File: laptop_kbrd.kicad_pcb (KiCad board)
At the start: 2 copper layers, 111.5 x 18 mm, 62 parts, among them CON1 AVR-ISP-6-DR, K1 CASE_OPEN, Q1 MOSFET_N, Q2 MOSFET_N, Q3 MOSFET_N, Q4 MOSFET_N, Q5 MOSFET_N, Q6 MOSFET_N, Q7 MOSFET_N, Q8 ALS_PT19, SW1 MCU_RST, SW2 BT_ASSCN, SW3 POWER, U1 ATMEGA32U4-AU, U2 RT9706, U3 RCLAMP0502B, U4 0WX4JF, U5 XF2M-3015-1A, X1 XTAL 16MHz

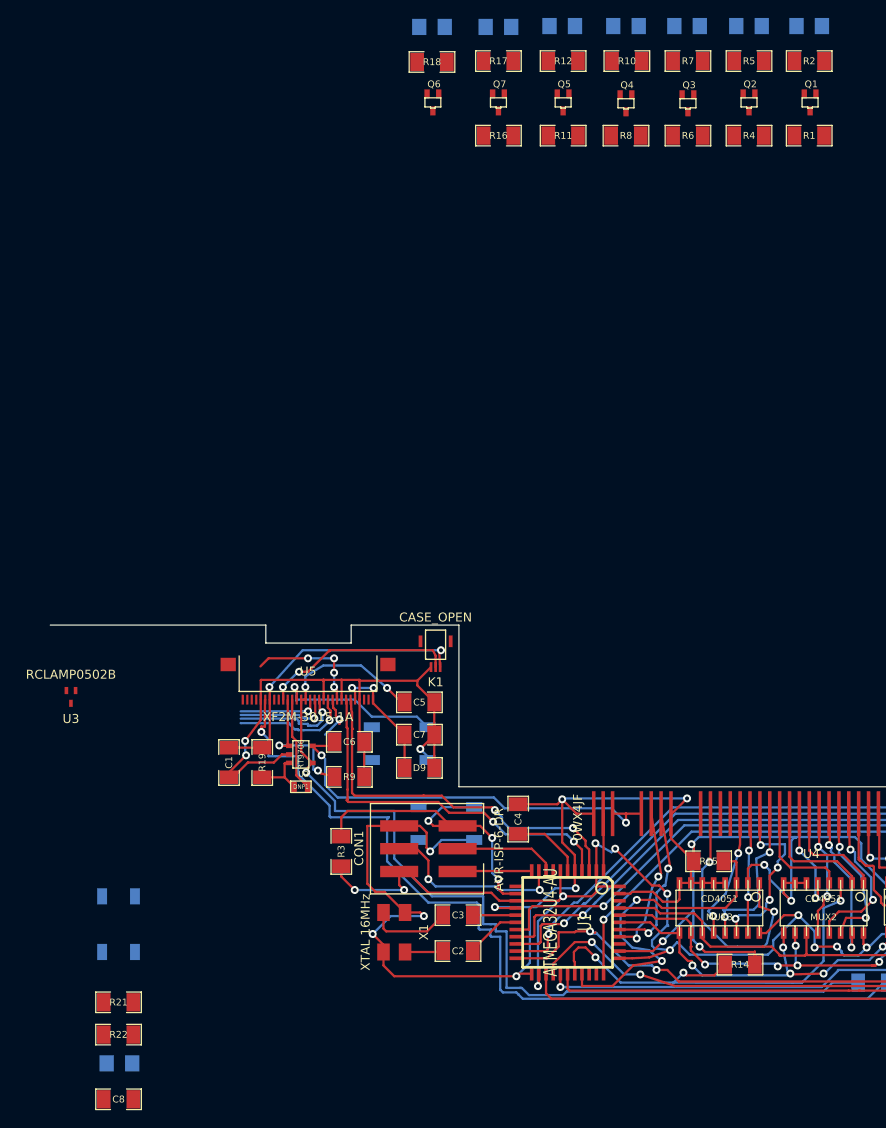
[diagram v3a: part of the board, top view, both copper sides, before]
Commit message: Removed RCLAMP
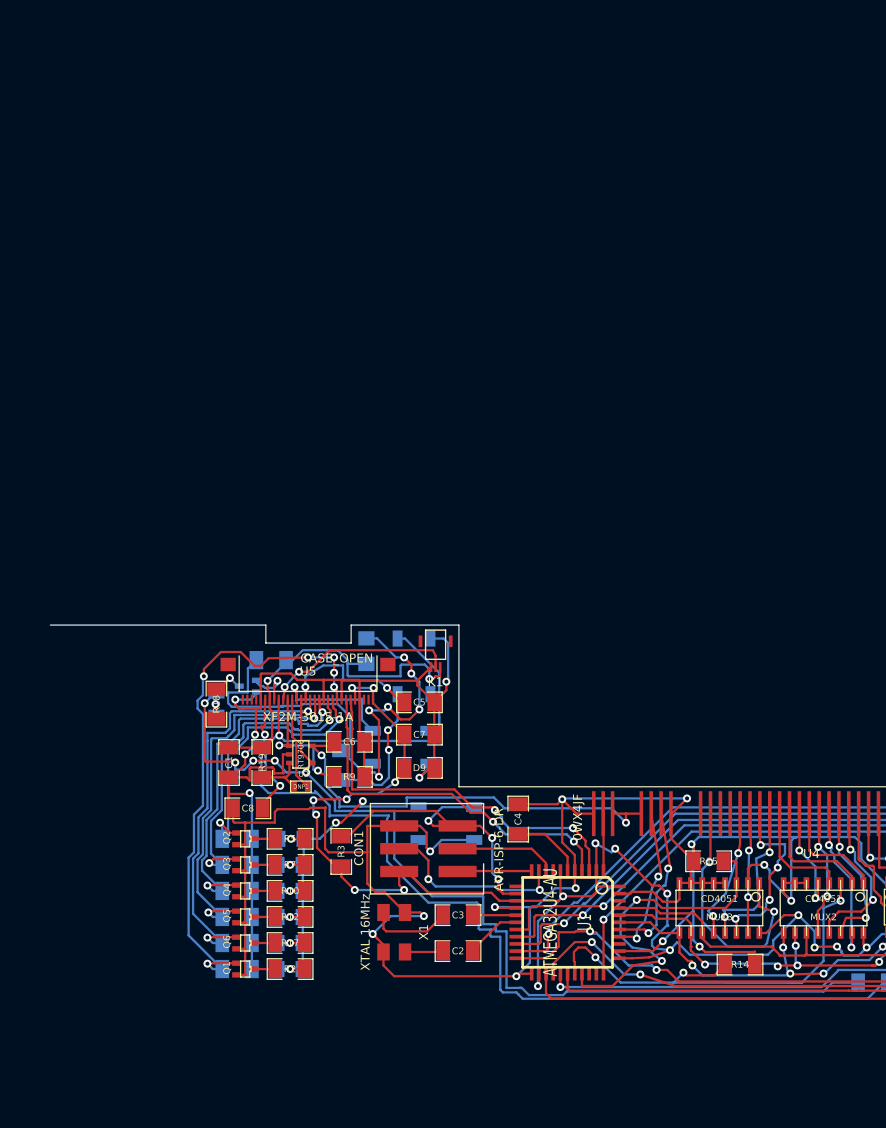
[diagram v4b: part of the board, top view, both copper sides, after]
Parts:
- removed U3: RCLAMP0502B, SOT523
- Q7, R1, R11, R16, R21, R22, R4, R6, R8: moved to B.Cu
- moved D1 119.9 mm to (91.2, 136.3), turned to 180 degrees
- moved R2 116.5 mm to (91.2, 136.3), turned to 180 degrees
- moved Q1 115.2 mm to (86.2, 136.3), turned to 90 degrees
- moved R1 112.6 mm to (85.3, 136.3)
- moved D6 104.6 mm to (91.2, 133.4), turned to 180 degrees
- moved D2 103.9 mm to (91.3, 121.8), turned to 180 degrees
- moved D5 103.7 mm to (91.2, 130.5), turned to 180 degrees
- moved D3 103.3 mm to (91.2, 124.7), turned to 180 degrees
- moved D4 103.3 mm to (91.2, 127.6), turned to 180 degrees
- moved R17 100.9 mm to (91.2, 133.4), turned to 180 degrees
- moved R5 100.6 mm to (91.2, 121.8), turned to 180 degrees
- moved R12 100.0 mm to (91.2, 130.5), turned to 180 degrees
- moved R7 99.9 mm to (91.2, 124.7), turned to 180 degrees
- moved R10 99.7 mm to (91.2, 127.6), turned to 180 degrees
- moved Q2 99.4 mm to (86.2, 121.8), turned to 90 degrees
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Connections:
- SW3 pad 3: (no net) -> /CHG_PWRSWITCH
- SW3 pad 4: /CHG_PWRSWITCH -> (no net)
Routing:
- net GND: track 320.2 -> 415.5 mm, vias 21 -> 24
- net /KEY_ROW1: track 0.00 -> 72.1 mm, vias 0 -> 2
- net /FPGA CLK: track 13.3 -> 62.5 mm, vias 4 -> 6
- net /FPGA CS: track 8.90 -> 45.2 mm, vias 1 -> 2
- net /FPGA HOLD: track 10.6 -> 42.5 mm, vias 1 -> 2
- net N-0000064: track 0.00 -> 31.7 mm, vias 0 -> 6
- net /FPGA MOSI: track 12.4 -> 40.3 mm, vias 1 -> 2
- net /FPGA WP: track 5.94 -> 32.3 mm, vias 1 -> 2
- net VDD: track 47.1 -> 72.9 mm, vias 2 -> 4
- net /FPGA MISO: track 13.3 -> 36.1 mm, vias 1 -> 2
- net /5V_DELAYED: track 107.2 -> 129.9 mm, vias 3 -> 7
- net VCC: track 148.2 -> 169.0 mm, vias 15 -> 19
- net N-0000065: track 0.00 -> 15.6 mm, vias 0 -> 2
- net /3.3V_DELAYED: track 33.7 -> 40.6 mm
- net /EPIT1_EPIT0: track 0.00 -> 5.64 mm, vias 0 -> 1
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
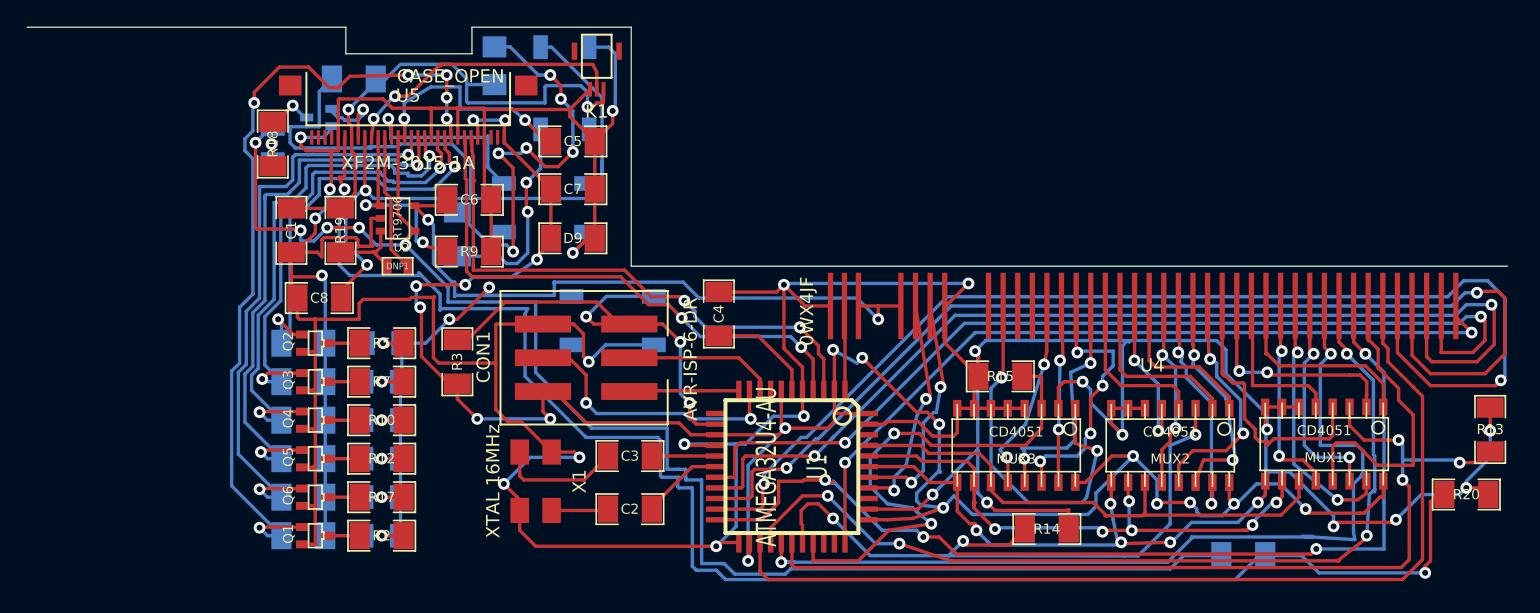
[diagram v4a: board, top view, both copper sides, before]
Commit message: Added lidsense. Mounting holes.
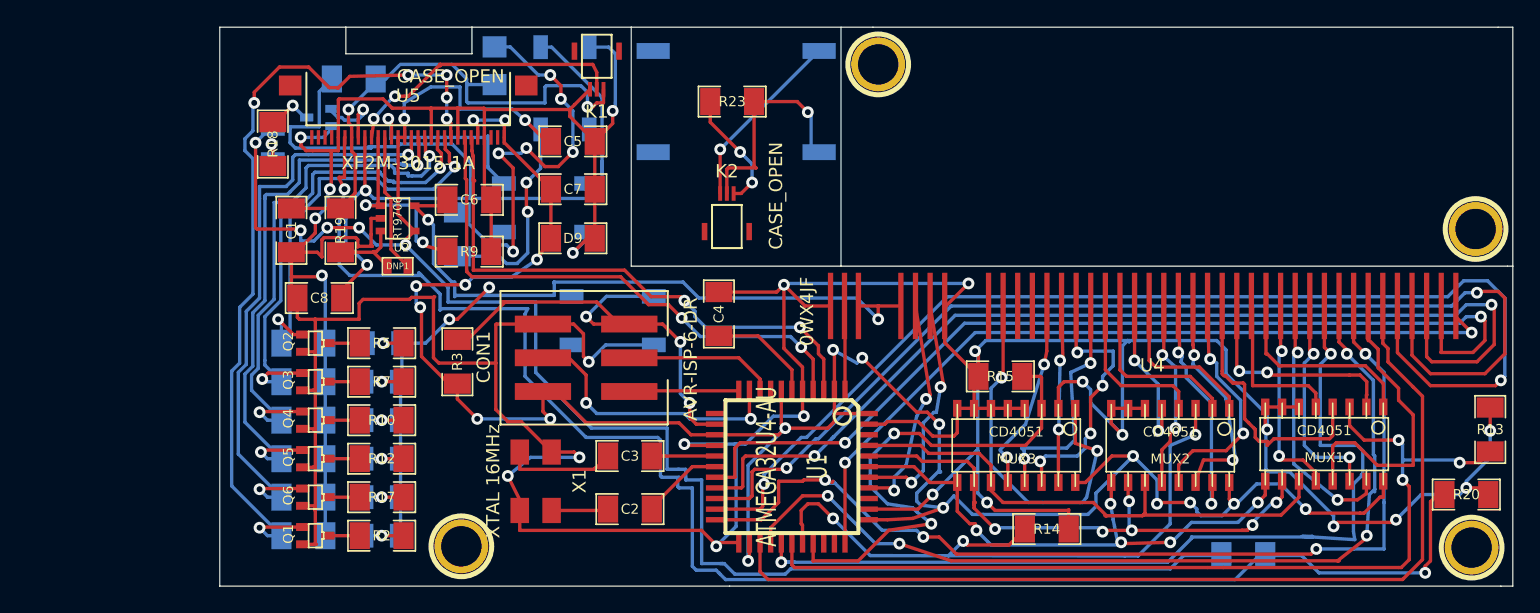
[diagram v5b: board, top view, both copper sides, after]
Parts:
- added ?: P***, 1pin, F.Cu at (173.3, 137.2)
- added ?: P***, 1pin, F.Cu at (97.2, 137.1)
- added ?: P***, 1pin, F.Cu at (128.6, 100.8)
- added ?: P***, 1pin, F.Cu at (173.6, 113.2)
- added K2: CASE_OPEN, 3pin_FPC, F.Cu at (117.2, 112.2)
- added R23: 47K, SM1206, F.Cu at (117.6, 103.6)
- added SW4: CASE_PUSH, PUSH_BT, B.Cu at (117.9, 103.6)
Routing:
- net N-0000060: track 0.00 -> 16.6 mm, vias 0 -> 1
- net N-0000059: track 0.00 -> 13.6 mm, vias 0 -> 1
- net N-0000057: track 0.00 -> 9.14 mm, vias 0 -> 2
- net N-0000010: track 9.32 -> 8.43 mm
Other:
- board size 111.5 x 18 mm -> 97.4 x 42.1 mm

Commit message: New components for the LCD controller.
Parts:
- added C10: 22pF, SM1206, F.Cu at (232.1, 176.1)
- added C11: 22pF, SM1206, F.Cu at (345.6, 72.3)
- added C12: 22pF, SM1206, F.Cu at (354.9, 72.8)
- added C13: 1uF, SM1206, F.Cu at (238.3, 165.2)
- added C14: 1uF, SM1206, F.Cu at (345.6, 69.7)
- added C15: 0.1uF, SM1206, F.Cu at (303.3, 217.6)
- added C16: 2.2nF, SM1206, F.Cu at (305.4, 213.0)
- added C17: 0.1uF, SM1206, F.Cu at (309.1, 197.9)
- added C18: 2.2nF, SM1206, F.Cu at (306.2, 223.1)
- added C19: 100pF, SM1206, F.Cu at (325.4, 222.6)
- added C20: 22pF, SM1206, F.Cu at (263.9, 171.2)
- added C21: 2.2nF, SM1206, F.Cu at (315.8, 228.8)
- added C22: 22pF, SM1206, F.Cu at (263.9, 168.5)
- added C23: 0.1uF, SM1206, F.Cu at (331.9, 217.0)
- added C24: 0.1uF, SM1206, F.Cu at (210.6, 176.4)
- added C9: 22pF, SM1206, F.Cu at (225.3, 176.1)
- added CON2: AVR-ISP-6-DR, AVR_6_SMD, B.Cu at (245.6, 165.2)
- added CON3: AVR-ISP-6-DR, AVR_6_SMD, B.Cu at (367.2, 66.9)
- added JP1: JUMPER, 2pin_JUMPER_SMD, F.Cu at (292.7, 224.2)
- added Q10: MOSFET_N, SOT323_DR, B.Cu at (214.8, 172.2)
- added Q11: MOSFET_N, SOT323_DR, B.Cu at (243.5, 176.2)
- added Q9: MOSFET_N, SOT323_DR, B.Cu at (335.4, 66.9)
- added R24: 10K, SM1206, F.Cu at (124.3, 103.1)
- added R25: 10K, SM1206, F.Cu at (244.8, 173.0)
- added R26: 10K, SM1206, F.Cu at (358.7, 72.8)
- added R27: 10K, SM1206, F.Cu at (228.8, 158.5)
- added R28: 10K, SM1206, F.Cu at (345.6, 66.8)
- added R29: 4.7K, SM1206, F.Cu at (301.8, 197.5)
- added R30: 1K, SM1206, F.Cu at (315.6, 205.1)
- added R31: 1K, SM1206, F.Cu at (316.5, 210.2)
- added R32: 500K, SM1206, F.Cu at (325.7, 212.7)
- added R33: 1.5K, SM1206, F.Cu at (263.9, 173.8)
- added R34: 500K, SM1206, F.Cu at (325.8, 207.0)
- added R35: 4.7K, SM1206, F.Cu at (324.9, 226.4)
- added R36: 10K, SM1206, F.Cu at (333.9, 70.8)
- added R37: 10K, SM1206, F.Cu at (218.6, 171.9)
- added R38: 10K, SM1206, F.Cu at (238.5, 174.7)
- added SW5: MCU_RST, TACT_SW, B.Cu at (215.2, 162.2)
- added SW6: MCU_RST, TACT_SW, B.Cu at (357.8, 74.2)
- added SW7: SPST, TEST_POINT_2PADS, F.Cu at (216.1, 178.0)
- added U10: NHD-0440AZ-FL-YBW, NHD_0440AZ_FL_YBW, F.Cu at (204.1, 167.8)
- added U11: NRF24L01+, 8pin_0.1inch, F.Cu at (235.6, 179.4)
- added U12: ATAES132A, so-8, F.Cu at (300.6, 203.7)
- added U13: AT97SC3205T, QFN32, F.Cu at (318.5, 217.4)
- added U14: TUSB2046BVFR, TQFP32, B.Cu at (263.9, 171.5)
- added U15: MAX6749, SOT23_8, F.Cu at (325.4, 218.9)
- added U16: BME280, BME280, F.Cu at (331.9, 206.8)
- added U17: TPS2041B, SOT23-5, B.Cu at (273.6, 167.4)
- added U18: LVDS_HEADER, 7pin_0.1inch, F.Cu at (223.8, 103.8)
- added U3: ATMEGA32U4, TQFP44, B.Cu at (229.0, 167.2)
- added U6: ATMEGA32U4, TQFP44, B.Cu at (345.5, 69.0)
- added U7: USB_CAM, 4pin_0.1inch, F.Cu at (315.0, 69.1)
- added U8: EPAPER_V2, EPAPER_V2, F.Cu at (326.6, 69.1)
- added U9: USB_A_FEMALE, USB_A, F.Cu at (264.9, 162.4)
- added X2: XTAL 16MHz, XTAL_6mmx3.5mm, F.Cu at (229.0, 167.4)
- added X3: XTAL 16MHz, XTAL_6mmx3.5mm, F.Cu at (356.3, 65.7)
- added X4: 6MHz, XTAL_HCM49, F.Cu at (255.1, 171.8)
- moved ? 48.8 mm to (139.2, 78.6)
- moved C2 38.3 mm to (125.9, 99.5)
- moved C3 38.3 mm to (125.9, 95.5)
- moved C8 38.3 mm to (102.5, 83.6)
- moved CON1 38.3 mm to (122.6, 88.1)
- moved D1 38.3 mm to (107.2, 101.5)
- moved D6 38.3 mm to (107.2, 98.6)
- moved D8 38.3 mm to (115.7, 66.1)
- moved D9 38.3 mm to (121.6, 79.1)
- moved MUX1 38.3 mm to (178.2, 94.6)
- moved Q1 38.3 mm to (102.2, 101.5)
- moved Q6 38.3 mm to (102.2, 98.6)
- moved Q8 38.3 mm to (172.1, 103.0)
- moved R1 38.3 mm to (101.3, 101.5)
- moved R13 38.3 mm to (190.7, 93.5)
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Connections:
- U1 pad 18: /P2 -> /P3
- U1 pad 19: /P3 -> /P4
- U1 pad 20: /P4 -> /P5
- U1 pad 21: /P5 -> /P6
- U1 pad 22: /P8 -> (no net)
- U1 pad 25: /P6 -> /P8
- U1 pad 31: (no net) -> /P1
- U1 pad 32: (no net) -> /P2
- U1 pad 33: /P1 -> N-0000062
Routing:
- net N-0000062: track 0.00 -> 22.4 mm, vias 0 -> 2
- net /P6: track 73.3 -> 83.9 mm, vias 0 -> 2
- net /P2: track 73.0 -> 69.6 mm
- net GND: track 415.2 -> 417.3 mm
- net /P8: track 74.4 -> 73.0 mm
- net /P4: track 83.2 -> 81.9 mm
- net /P9: track 68.8 -> 69.9 mm
- net /P3: track 78.3 -> 79.3 mm
- net /P1: track 59.8 -> 60.7 mm
- net /P5: track 87.2 -> 86.5 mm
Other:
- board size 97.4 x 42.1 mm -> 208.5 x 42.1 mm

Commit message: Gerbers left to be created.
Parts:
- C15, C16, C17, C19, C21, C23, JP1, R29, R30, R31: moved to B.Cu
- Q10, Q11, U17: moved to F.Cu
- U13: footprint QFN32 -> QFN32_DR
- U9: footprint USB_A -> USB_A_DR; moved to B.Cu
- moved U15 182.4 mm to (207.1, 80.1), turned to 0 degrees
- moved R35 180.5 mm to (230.4, 72.6), turned to 90 degrees
- moved C21 180.5 mm to (222.9, 74.1)
- moved C19 180.1 mm to (213.4, 81.5), turned to 0 degrees
- moved C23 179.4 mm to (234.5, 66.4), turned to 270 degrees
- moved C15 177.0 mm to (208.9, 67.9), turned to 180 degrees
- moved U13 176.7 mm to (214.7, 74.4)
- moved Q9 175.9 mm to (159.5, 69.6)
- moved R26 175.7 mm to (183.0, 74.6)
- moved X3 175.2 mm to (181.1, 67.2)
- moved C18 175.1 mm to (221.5, 69.8), turned to 270 degrees
- moved R36 174.5 mm to (159.4, 71.8)
- moved CON3 173.4 mm to (193.8, 68.5)
- moved SW6 173.2 mm to (184.6, 74.3), turned to 270 degrees
- moved C11 172.2 mm to (173.4, 75.7)
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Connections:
- U3 pad 3: /LCD_board/D1- -> /LCD_board/D4-
- U3 pad 4: /LCD_board/D1+ -> /LCD_board/D4+
- U9 pad 2: /LCD_board/D4+ -> /LCD_board/D1+
- U9 pad 3: /LCD_board/D4- -> /LCD_board/D1-
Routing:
- net /LCD_board/GND2: track 0.00 -> 444.4 mm, vias 0 -> 25
- net /LCD_board/Vcc2: track 0.00 -> 248.9 mm, vias 0 -> 16
- net /LCD_board/V3.32: track 0.00 -> 224.4 mm, vias 0 -> 12
- net /LCD_board/D3-: track 0.00 -> 69.3 mm, vias 0 -> 2
- net /LCD_board/D3+: track 0.00 -> 68.7 mm
- net /LCD_board/MOSI_A: track 0.00 -> 60.8 mm, vias 0 -> 3
- net /LCD_board/MOSI_B: track 0.00 -> 59.8 mm, vias 0 -> 3
- net /LCD_board/MISO_B: track 0.00 -> 59.4 mm, vias 0 -> 1
- net /LCD_board/D4-: track 0.00 -> 55.8 mm, vias 0 -> 4
- net /LCD_board/SCK_B: track 0.00 -> 54.9 mm, vias 0 -> 1
- net /LCD_board/VUSB4: track 0.00 -> 50.2 mm
- net /LCD_board/SCK_A: track 0.00 -> 49.8 mm, vias 0 -> 4
- net /LCD_board/D4+: track 0.00 -> 48.7 mm, vias 0 -> 4
- net /LCD_board/MISO_A: track 0.00 -> 47.6 mm, vias 0 -> 2
- net /LCD_board/~RST: track 0.00 -> 43.5 mm, vias 0 -> 7
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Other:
- board size 208.5 x 42.1 mm -> 141.3 x 42.1 mm
